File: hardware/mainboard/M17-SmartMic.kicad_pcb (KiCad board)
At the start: 4 copper layers, 99.5 x 80 mm, 203 parts, among them IC301 LM4991MA, J301 CAT_TX, J302 CAT_RX, J401 Radio, J402 USB_C, J403 Radio_Opt, J404 Kenwood-3.5, J405 Kenwood-2.5, J406 2.54mm Header 7p, J407 KH-RJ45-58-8P8C, J408 STLink, J409 UART, J410 Speaker, J411 +12V, J412 Hirose FH12-26S-0.5SH(55), J413 Molex 532610271, Q201 MMBT3904, Q202 IRLML2244, Q301 IRLML2060, Q302 BSS138, Q303 BSS138, SW201 Tactile switch, SW202 Tactile switch, SW203 Tactile switch, SW204 Tactile switch, SW205 Tactile switch, SW206 Tactile switch, SW207 Tactile switch, SW208 Tactile switch, U201 STM32F405RGTx, U202 TPS7A2033, U203 TP6841S6, U301 MCP6002, U302 MAX9814, U401 USBLC6-2SC6, U501 MCP4551-103, U502 MCP4551-103, U503 MCP6002, U504 MCP6002, Y201 8 MHz

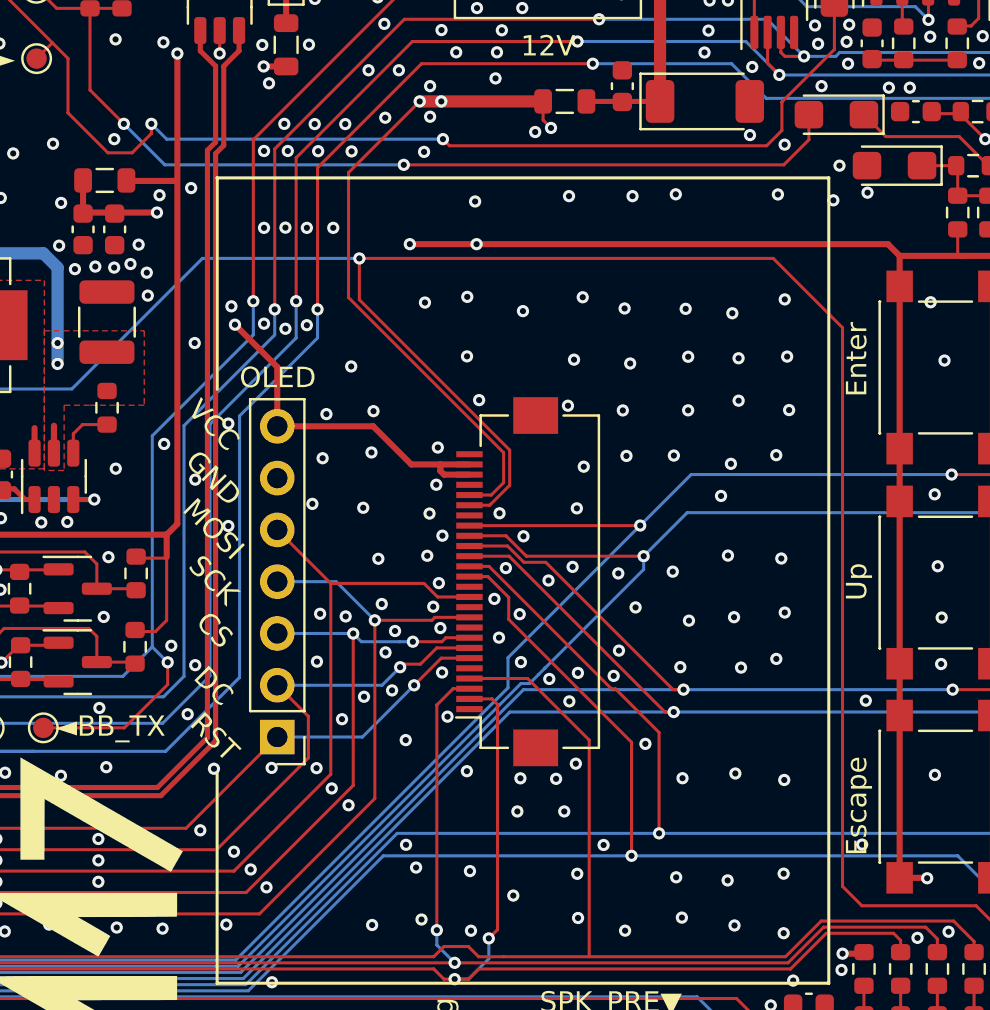
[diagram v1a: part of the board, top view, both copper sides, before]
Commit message: Updated HMI_PWR_ON and Net-(510-Pad2) layout
moved trace to keep a gnd sliver around, placed a few vias
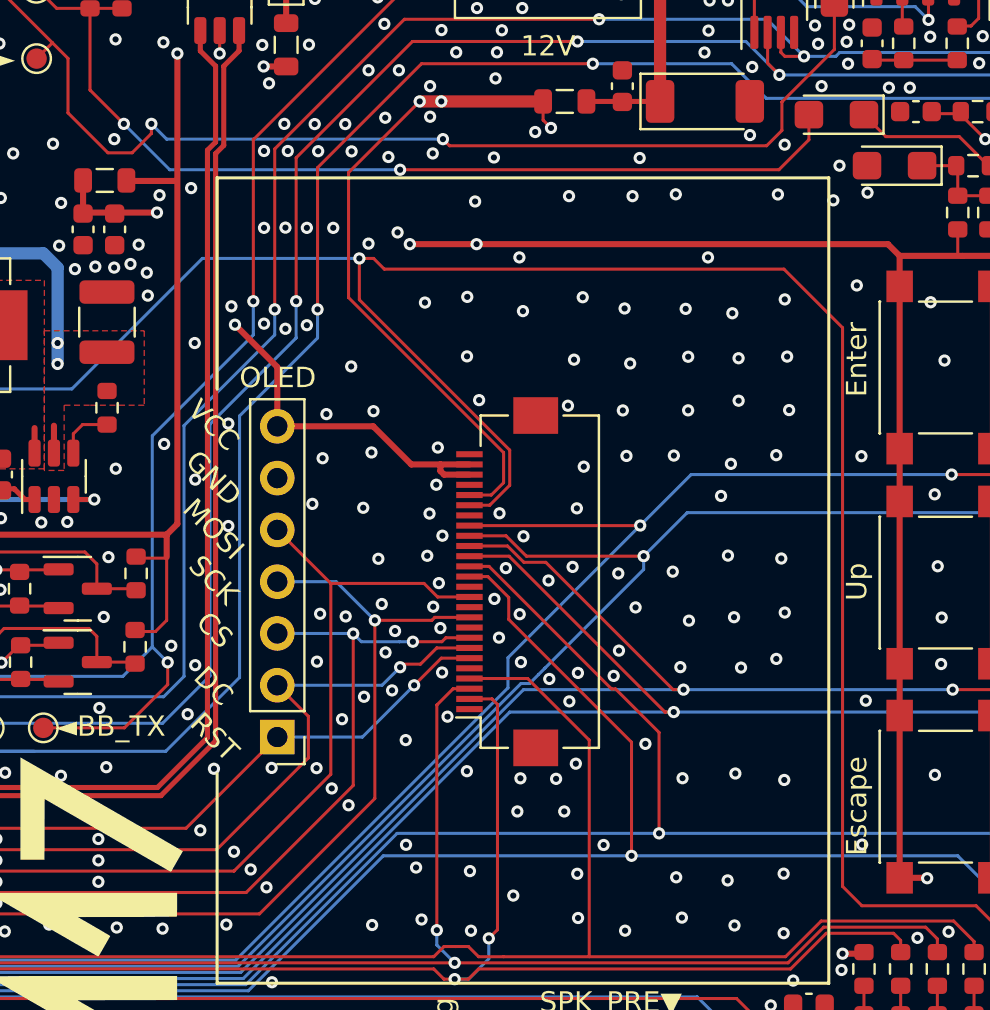
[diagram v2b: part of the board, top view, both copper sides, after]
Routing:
- net GND: vias 1055 -> 1064
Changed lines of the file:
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@@
   (via (at 214.175 74.425) (size 0.6) (drill 0.3) (layers "F.Cu" "B.Cu") (free) (net 2))
   (via (at 188.166622 110.841622) (size 0.6) (drill 0.3) (layers "F.Cu" "B.Cu") (free) (net 2))
+  (via (at 231.15 67.65) (size 0.6) (drill 0.3) (layers "F.Cu" "B.Cu") (free) (net 2))
   (via (at 199.775 97.313) (size 0.6) (drill 0.3) (layers "F.Cu" "B.Cu") (free) (net 2))
   (via (at 269.15 104.575) (size 0.6) (drill 0.3) (layers "F.Cu" "B.Cu") (free) (net 2))
@@
   (via (at 253.45 105.625) (size 0.6) (drill 0.3) (layers "F.Cu" "B.Cu") (free) (net 2))
   (via (at 185.4 98.35) (size 0.6) (drill 0.3) (layers "F.Cu" "B.Cu") (free) (net 2))
+  (via (at 225 71.875) (size 0.6) (drill 0.3) (layers "F.Cu" "B.Cu") (free) (net 2))
   (via (at 182.55 111.425) (size 0.6) (drill 0.3) (layers "F.Cu" "B.Cu") (free) (net 2))
   (via (at 211.75 103.1755) (size 0.6) (drill 0.3) (layers "F.Cu" "B.Cu") (free) (net 2))
@@
   (via (at 268.15 97.075) (size 0.6) (drill 0.3) (layers "F.Cu" "B.Cu") (free) (net 2))
   (via (at 170.85 99.575) (size 0.6) (drill 0.3) (layers "F.Cu" "B.Cu") (free) (net 2))
+  (via (at 238.3 67.675) (size 0.6) (drill 0.3) (layers "F.Cu" "B.Cu") (free) (net 2))
   (via (at 193 69.825) (size 0.6) (drill 0.3) (layers "F.Cu" "B.Cu") (free) (net 2))
   (via (at 261.4 52.425) (size 0.6) (drill 0.3) (layers "F.Cu" "B.Cu") (free) (net 2))
@@
   (via (at 216.5 83.45) (size 0.6) (drill 0.3) (layers "F.Cu" "B.Cu") (free) (net 2))
   (via (at 203.35 114.8595) (size 0.6) (drill 0.3) (layers "F.Cu" "B.Cu") (free) (net 2))
+  (via (at 225.975 67.625) (size 0.6) (drill 0.3) (layers "F.Cu" "B.Cu") (free) (net 2))
   (via (at 233.175 66.4) (size 0.6) (drill 0.3) (layers "F.Cu" "B.Cu") (free) (net 2))
   (via (at 225.82 65.7) (size 0.6) (drill 0.3) (layers "F.Cu" "B.Cu") (free) (net 2))
@@
   (via (at 225.18 54.19) (size 0.6) (drill 0.3) (layers "F.Cu" "B.Cu") (free) (net 2))
   (via (at 252.588603 115.710207) (size 0.6) (drill 0.3) (layers "F.Cu" "B.Cu") (free) (net 2))
+  (via (at 232.4 72.55) (size 0.6) (drill 0.3) (layers "F.Cu" "B.Cu") (free) (net 2))
   (via (at 269.15 109.575) (size 0.6) (drill 0.3) (layers "F.Cu" "B.Cu") (free) (net 2))
+  (via (at 241.65 72.55) (size 0.6) (drill 0.3) (layers "F.Cu" "B.Cu") (free) (net 2))
   (via (at 198.645023 66.295023) (size 0.6) (drill 0.3) (layers "F.Cu" "B.Cu") (free) (net 2))
   (via (at 242.950294 105.31586) (size 0.6) (drill 0.3) (layers "F.Cu" "B.Cu") (free) (net 2))
@@
   (via (at 186.774071 125.569745) (size 0.6) (drill 0.3) (layers "F.Cu" "B.Cu") (free) (net 2))
   (via (at 213.7 56.5) (size 0.6) (drill 0.3) (layers "F.Cu" "B.Cu") (free) (net 2))
+  (via (at 226.425 71.325) (size 0.6) (drill 0.3) (layers "F.Cu" "B.Cu") (free) (net 2))
   (via (at 197.504683 56.748891) (size 0.6) (drill 0.3) (layers "F.Cu" "B.Cu") (free) (net 2))
   (via (at 234.931485 49.146212) (size 0.6) (drill 0.3) (layers "F.Cu" "B.Cu") (free) (net 2))
@@
   (via (at 232.6005 86.2295) (size 0.6) (drill 0.3) (layers "F.Cu" "B.Cu") (free) (net 2))
   (via (at 241.48 62.5) (size 0.6) (drill 0.3) (layers "F.Cu" "B.Cu") (free) (net 2))
+  (via (at 249.175 82.3) (size 0.6) (drill 0.3) (layers "F.Cu" "B.Cu") (free) (net 2))
   (via (at 170.85 119.575) (size 0.6) (drill 0.3) (layers "F.Cu" "B.Cu") (free) (net 2))
   (via (at 269.15 122.575) (size 0.6) (drill 0.3) (layers "F.Cu" "B.Cu") (free) (net 2))
@@
   (via (at 204.821 80.2) (size 0.6) (drill 0.3) (layers "F.Cu" "B.Cu") (free) (net 2))
   (via (at 269.15 108.575) (size 0.6) (drill 0.3) (layers "F.Cu" "B.Cu") (free) (net 2))
-  (via (at 227.725 67.375) (size 0.6) (drill 0.3) (layers "F.Cu" "B.Cu") (free) (net 2))
+  (via (at 228.15 67.45) (size 0.6) (drill 0.3) (layers "F.Cu" "B.Cu") (free) (net 2))
   (via (at 185.35 83.85) (size 0.6) (drill 0.3) (layers "F.Cu" "B.Cu") (free) (net 2))
   (via (at 260.438095 80.410222) (size 0.6) (drill 0.3) (layers "F.Cu" "B.Cu") (free) (net 2))
@@
   (via (at 176.125 109.425) (size 0.6) (drill 0.3) (layers "F.Cu" "B.Cu") (free) (net 2))
   (via (at 211.51 55.24) (size 0.6) (drill 0.3) (layers "F.Cu" "B.Cu") (free) (net 2))
+  (via (at 248.95 73.925) (size 0.6) (drill 0.3) (layers "F.Cu" "B.Cu") (free) (net 2))
   (via (at 199.75 94.85) (size 0.6) (drill 0.3) (layers "F.Cu" "B.Cu") (free) (net 2))
   (via (at 218.142694 57.907306) (size 0.6) (drill 0.3) (layers "F.Cu" "B.Cu") (free) (net 2))
@@
   (segment (start 181.2 85.2) (end 189.05 93.05) (width 0.15) (layer "B.Cu") (net 53))
   (segment (start 181.2 80.6) (end 181.2 85.2) (width 0.15) (layer "B.Cu") (net 53))
+  (segment (start 226.55 68.25) (end 245.13 68.25) (width 0.15) (layer "F.Cu") (net 54))
   (segment (start 211.34 60.335) (end 212.91 60.335) (width 0.15) (layer "F.Cu") (net 54))
   (segment (start 209.705 60.335) (end 211.34 60.335) (width 0.15) (layer "F.Cu") (net 54))
+  (segment (start 246.6 66.78) (end 246.6 65.55) (width 0.15) (layer "F.Cu") (net 54))
   (segment (start 208.71 59.35) (end 208.72 59.35) (width 0.15) (layer "F.Cu") (net 54))
-  (segment (start 226.73 68.01) (end 245.37 68.01) (width 0.15) (layer "F.Cu") (net 54))
   (segment (start 213 66) (end 211.34 64.34) (width 0.15) (layer "F.Cu") (net 54))
   (segment (start 211.34 64.34) (end 211.34 60.46) (width 0.15) (layer "F.Cu") (net 54))
-  (segment (start 246.6 66.78) (end 246.6 65.55) (width 0.15) (layer "F.Cu") (net 54))
+  (segment (start 245.13 68.25) (end 246.6 66.78) (width 0.15) (layer "F.Cu") (net 54))
   (segment (start 208.72 59.35) (end 209.705 60.335) (width 0.15) (layer "F.Cu") (net 54))
-  (segment (start 245.37 68.01) (end 246.6 66.78) (width 0.15) (layer "F.Cu") (net 54))
   (via (at 213 66) (size 0.6) (drill 0.3) (layers "F.Cu" "B.Cu") (net 54))
-  (via (at 226.73 68.01) (size 0.6) (drill 0.3) (layers "F.Cu" "B.Cu") (net 54))
-  (segment (start 226.73 68.01) (end 215.01 68.01) (width 0.15) (layer "B.Cu") (net 54))
-  (segment (start 215.01 68.01) (end 213 66) (width 0.15) (layer "B.Cu") (net 54))
+  (via (at 226.55 68.25) (size 0.6) (drill 0.3) (layers "F.Cu" "B.Cu") (net 54))
+  (segment (start 226.55 68.25) (end 215.25 68.25) (width 0.15) (layer "B.Cu") (net 54))
+  (segment (start 215.25 68.25) (end 213 66) (width 0.15) (layer "B.Cu") (net 54))
   (segment (start 257.535 93.11) (end 257.535 93.49) (width 0.15) (layer "F.Cu") (net 55))
   (segment (start 233.695 87.505) (end 232.619264 87.505) (width 0.15) (layer "F.Cu") (net 55))
@@
   (segment (start 220.96 61.06) (end 220.96 59.59) (width 0.3) (layer "F.Cu") (net 148))
   (segment (start 231.925 82) (end 224.55 74.625) (width 0.15) (layer "F.Cu") (net 149))
-  (segment (start 248.25 85.2) (end 248.25 103.4) (width 0.15) (layer "F.Cu") (net 149))
-  (segment (start 224.55 72.6) (end 244.85 72.6) (width 0.15) (layer "F.Cu") (net 149))
+  (segment (start 249.2 104.35) (end 254.8 104.35) (width 0.15) (layer "F.Cu") (net 149))
+  (segment (start 257.25 105.425) (end 257.55 105.125) (width 0.15) (layer "F.Cu") (net 149))
+  (segment (start 245.375 73.125) (end 248.25 76) (width 0.15) (layer "F.Cu") (net 149))
+  (segment (start 248.25 103.4) (end 249.2 104.35) (width 0.15) (layer "F.Cu") (net 149))
   (segment (start 230.944264 84.705) (end 231.925 83.724264) (width 0.15) (layer "F.Cu") (net 149))
   (segment (start 264.15 114.38) (end 264.15 106.42) (width 0.15) (layer "F.Cu") (net 149))
   (segment (start 188.775 71.3) (end 189.85 71.3) (width 0.15) (layer "F.Cu") (net 149))
+  (segment (start 255.875 105.425) (end 257.25 105.425) (width 0.15) (layer "F.Cu") (net 149))
+  (segment (start 229.95 84.705) (end 230.944264 84.705) (width 0.15) (layer "F.Cu") (net 149))
+  (segment (start 248.25 76) (end 248.25 103.4) (width 0.15) (layer "F.Cu") (net 149))
+  (segment (start 225.25 72.6) (end 225.775 73.125) (width 0.15) (layer "F.Cu") (net 149))
+  (segment (start 224.55 74.625) (end 224.55 72.6) (width 0.15) (layer "F.Cu") (net 149))
+  (segment (start 225.775 73.125) (end 245.375 73.125) (width 0.15) (layer "F.Cu") (net 149))
+  (segment (start 224.55 72.6) (end 225.25 72.6) (width 0.15) (layer "F.Cu") (net 149))
+  (segment (start 231.925 83.724264) (end 231.925 82) (width 0.15) (layer "F.Cu") (net 149))
   (segment (start 254.8 104.35) (end 255.875 105.425) (width 0.15) (layer "F.Cu") (net 149))
-  (segment (start 248.25 103.4) (end 249.2 104.35) (width 0.15) (layer "F.Cu") (net 149))
-  (segment (start 244.85 72.6) (end 248.25 76) (width 0.15) (layer "F.Cu") (net 149))
-  (segment (start 248.25 76) (end 248.25 85.2) (width 0.15) (layer "F.Cu") (net 149))
-  (segment (start 229.95 84.705) (end 230.944264 84.705) (width 0.15) (layer "F.Cu") (net 149))
-  (segment (start 224.55 74.625) (end 224.55 72.6) (width 0.15) (layer "F.Cu") (net 149))
+  (segment (start 257.55 105.125) (end 262.855 105.125) (width 0.15) (layer "F.Cu") (net 149))
   (segment (start 262.855 105.125) (end 264.15 106.42) (width 0.15) (layer "F.Cu") (net 149))
-  (segment (start 257.55 105.125) (end 262.855 105.125) (width 0.15) (layer "F.Cu") (net 149))
-  (segment (start 249.2 104.35) (end 254.8 104.35) (width 0.15) (layer "F.Cu") (net 149))
-  (segment (start 231.925 83.724264) (end 231.925 82) (width 0.15) (layer "F.Cu") (net 149))
-  (segment (start 255.875 105.425) (end 257.25 105.425) (width 0.15) (layer "F.Cu") (net 149))
-  (segment (start 257.25 105.425) (end 257.55 105.125) (width 0.15) (layer "F.Cu") (net 149))
   (via (at 224.55 72.6) (size 0.6) (drill 0.3) (layers "F.Cu" "B.Cu") (net 149))
   (via (at 188.775 71.3) (size 0.6) (drill 0.3) (layers "F.Cu" "B.Cu") (net 149))

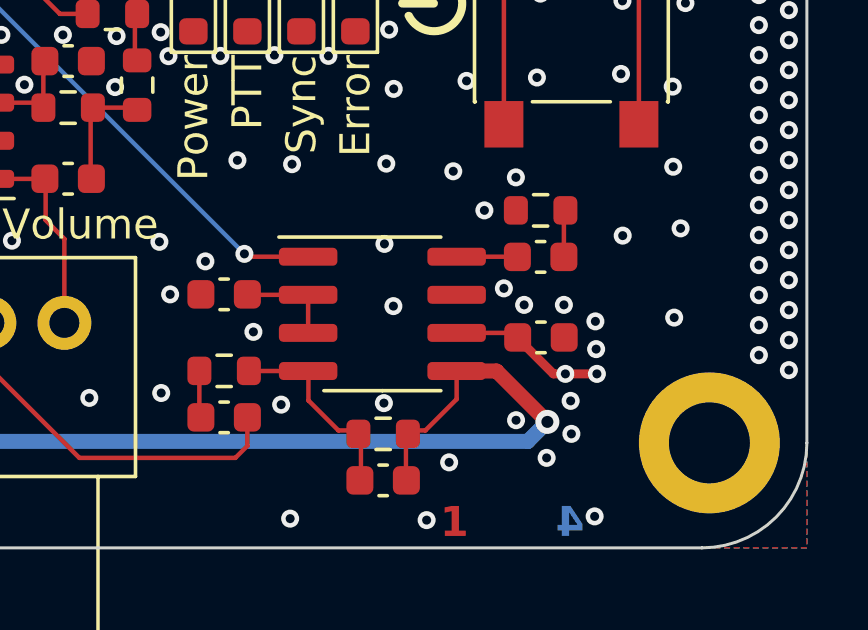
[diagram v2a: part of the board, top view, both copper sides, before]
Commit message: Added pull-up to SPK_MUTE
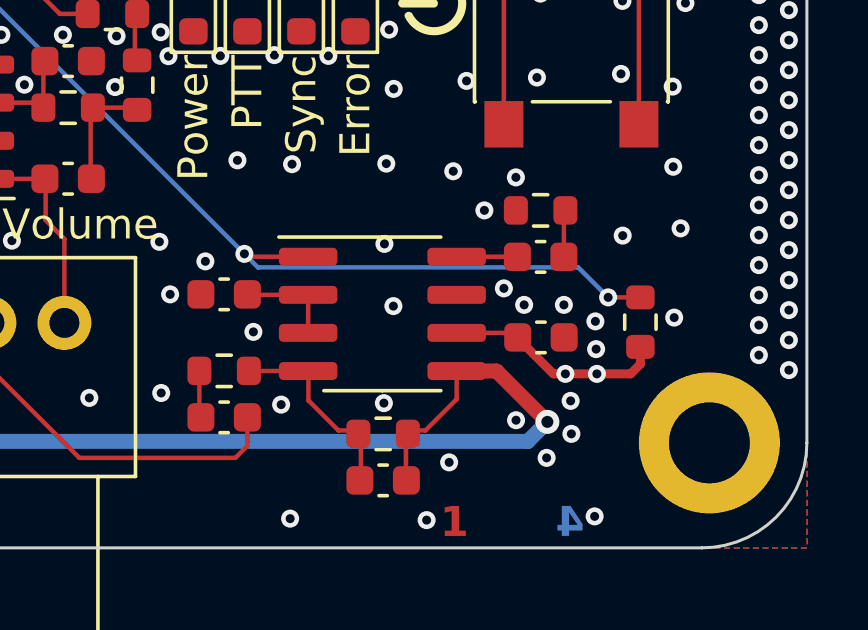
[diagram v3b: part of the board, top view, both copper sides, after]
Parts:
- added R319: 10k, Resistor_SMD:R_0603_1608Metric, F.Cu at (264.2, 121.0)
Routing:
- net SPK_MUTE: track 69.6 -> 83.4 mm, vias 2 -> 3
- net +5V: track 237.1 -> 239.3 mm
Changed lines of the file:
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@@
   )
   (footprint "Resistor_SMD:R_0603_1608Metric" (layer "F.Cu")
+    (at 264.2 120.975 -90)
+    (descr "Resistor SMD 0603 (1608 Metric), square (rectangular) end terminal, IPC_7351 nominal, (Body size source: IPC-SM-782 page 72, https://www.pcb-3d.com/wordpress/wp-content/uploads/ipc-sm-782a_amendment_1_and_2.pdf), generated with kicad-footprint-generator")
+    (tags "resistor")
+    (property "MPN" "Generic R/10k/0603")
+    (property "Sheetfile" "Audio.kicad_sch")
+    (property "Sheetname" "Audio & Filter")
+    (property "ki_description" "Resistor, small symbol")
+    (property "ki_keywords" "R resistor")
+    (attr smd)
+    (fp_text reference "R319" (at 0 -1.43 90) (layer "F.Fab")
+        (effects (font (size 1 1) (thickness 0.15)))
+    )
+    (fp_text value "10k" (at 0 1.43 90) (layer "F.Fab")
+        (effects (font (size 1 1) (thickness 0.15)))
+    )
+    (fp_text user "${REFERENCE}" (at 0 0 90) (layer "F.Fab")
+        (effects (font (size 0.4 0.4) (thickness 0.06)))
+    )
+    (fp_line (start -0.237258 -0.5225) (end 0.237258 -0.5225)
+      (stroke (width 0.12) (type solid)) (layer "F.SilkS"))
+    (fp_line (start -0.237258 0.5225) (end 0.237258 0.5225)
+      (stroke (width 0.12) (type solid)) (layer "F.SilkS"))
+    (fp_line (start -1.48 -0.73) (end 1.48 -0.73)
+      (stroke (width 0.05) (type solid)) (layer "F.CrtYd"))
+    (fp_line (start -1.48 0.73) (end -1.48 -0.73)
+      (stroke (width 0.05) (type solid)) (layer "F.CrtYd"))
+    (fp_line (start 1.48 -0.73) (end 1.48 0.73)
+      (stroke (width 0.05) (type solid)) (layer "F.CrtYd"))
+    (fp_line (start 1.48 0.73) (end -1.48 0.73)
+      (stroke (width 0.05) (type solid)) (layer "F.CrtYd"))
+    (fp_line (start -0.8 -0.4125) (end 0.8 -0.4125)
+      (stroke (width 0.1) (type solid)) (layer "F.Fab"))
+    (fp_line (start -0.8 0.4125) (end -0.8 -0.4125)
+      (stroke (width 0.1) (type solid)) (layer "F.Fab"))
+    (fp_line (start 0.8 -0.4125) (end 0.8 0.4125)
+      (stroke (width 0.1) (type solid)) (layer "F.Fab"))
+    (fp_line (start 0.8 0.4125) (end -0.8 0.4125)
+      (stroke (width 0.1) (type solid)) (layer "F.Fab"))
+    (pad "1" smd roundrect (at -0.825 0 270) (size 0.8 0.95) (layers "F.Cu" "F.Paste" "F.Mask") (roundrect_rratio 0.25)
+      (net 80 "SPK_MUTE") (pintype "passive"))
+    (pad "2" smd roundrect (at 0.825 0 270) (size 0.8 0.95) (layers "F.Cu" "F.Paste" "F.Mask") (roundrect_rratio 0.25)
+      (net 7 "+5V") (pintype "passive"))
+    (model "${KICAD6_3DMODEL_DIR}/Resistor_SMD.3dshapes/R_0603_1608Metric.wrl"
+      (offset (xyz 0 0 0))
+      (scale (xyz 1 1 1))
+      (rotate (xyz 0 0 0))
+    )
+  )
+  (footprint "Resistor_SMD:R_0603_1608Metric" (layer "F.Cu")
     (at 207.95 116.625 90)
     (descr "Resistor SMD 0603 (1608 Metric), square (rectangular) end terminal, IPC_7351 nominal, (Body size source: IPC-SM-782 page 72, https://www.pcb-3d.com/wordpress/wp-content/uploads/ipc-sm-782a_amendment_1_and_2.pdf), generated with kicad-footprint-generator")
@@
   (segment (start 262.75 122.7) (end 261.7 122.7) (width 0.3) (layer "F.Cu") (net 7))
   (segment (start 260.135 121.535) (end 260.135 121.485) (width 0.3) (layer "F.Cu") (net 7))
+  (segment (start 262.75 122.7) (end 263.875 122.7) (width 0.3) (layer "F.Cu") (net 7))
   (segment (start 194.7 83.15) (end 194.771 83.15) (width 0.3) (layer "F.Cu") (net 7))
   (segment (start 215.625 85.625) (end 215.1 86.15) (width 0.3) (layer "F.Cu") (net 7))
@@
   (segment (start 194.771 83.15) (end 194.7585 83.1375) (width 0.4) (layer "F.Cu") (net 7))
   (segment (start 204.8 86.15) (end 215.1 86.15) (width 0.3) (layer "F.Cu") (net 7))
+  (segment (start 264.2 122.375) (end 264.2 121.8) (width 0.3) (layer "F.Cu") (net 7))
   (segment (start 196.6 80.7) (end 197.35 80.7) (width 0.4) (layer "F.Cu") (net 7))
   (segment (start 213.55 90.9) (end 214.55 90.9) (width 0.15) (layer "F.Cu") (net 7))
+  (segment (start 263.875 122.7) (end 264.2 122.375) (width 0.3) (layer "F.Cu") (net 7))
   (segment (start 196.05 78.8) (end 194.7875 78.8) (width 0.15) (layer "F.Cu") (net 7))
   (segment (start 196.6 80.7) (end 196.5 80.6) (width 0.15) (layer "F.Cu") (net 7))
@@
   (segment (start 183.475 86.375) (end 184.05 86.375) (width 0.15) (layer "B.Cu") (net 78))
   (segment (start 252.9 109.3) (end 252.9 108.2) (width 0.15) (layer "F.Cu") (net 79))
+  (segment (start 264.2 120.15) (end 263.125 120.15) (width 0.15) (layer "F.Cu") (net 80))
   (segment (start 190.75 104.5) (end 190.75 105.7625) (width 0.15) (layer "F.Cu") (net 80))
   (segment (start 253.125 118.795) (end 251.095 118.795) (width 0.15) (layer "F.Cu") (net 80))
   (segment (start 251.095 118.795) (end 251 118.7) (width 0.15) (layer "F.Cu") (net 80))
+  (via (at 263.125 120.15) (size 0.6) (drill 0.3) (layers "F.Cu" "B.Cu") (net 80))
   (via (at 190.75 104.5) (size 0.6) (drill 0.3) (layers "F.Cu" "B.Cu") (net 80))
   (via (at 251 118.7) (size 0.6) (drill 0.3) (layers "F.Cu" "B.Cu") (net 80))
+  (segment (start 251.45 119.15) (end 251 118.7) (width 0.15) (layer "B.Cu") (net 80))
   (segment (start 195.95 106.6) (end 198.17 108.82) (width 0.15) (layer "B.Cu") (net 80))
   (segment (start 241.12 108.82) (end 251 118.7) (width 0.15) (layer "B.Cu") (net 80))
+  (segment (start 262.125 119.15) (end 251.45 119.15) (width 0.15) (layer "B.Cu") (net 80))
   (segment (start 192.85 106.6) (end 195.95 106.6) (width 0.15) (layer "B.Cu") (net 80))
   (segment (start 198.17 108.82) (end 241.12 108.82) (width 0.15) (layer "B.Cu") (net 80))
+  (segment (start 263.125 120.15) (end 262.125 119.15) (width 0.15) (layer "B.Cu") (net 80))
   (segment (start 190.75 104.5) (end 192.85 106.6) (width 0.15) (layer "B.Cu") (net 80))
   (segment (start 209.7 93.25) (end 203.475 93.25) (width 0.15) (layer "F.Cu") (net 81))
